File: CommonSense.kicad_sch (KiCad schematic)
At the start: 33 parts, among them J1 Conn_02x04_Counter_Clockwise, J2 Conn_01x02, J3 Conn_01x02, U1 NRF52810-QFAA-R7, U2 SHT41-AD1B-R2, Y1 ECS-.327-12.5-12R-TR, Y2 ABM11W-32.0000MHZ-7-D1X-T3

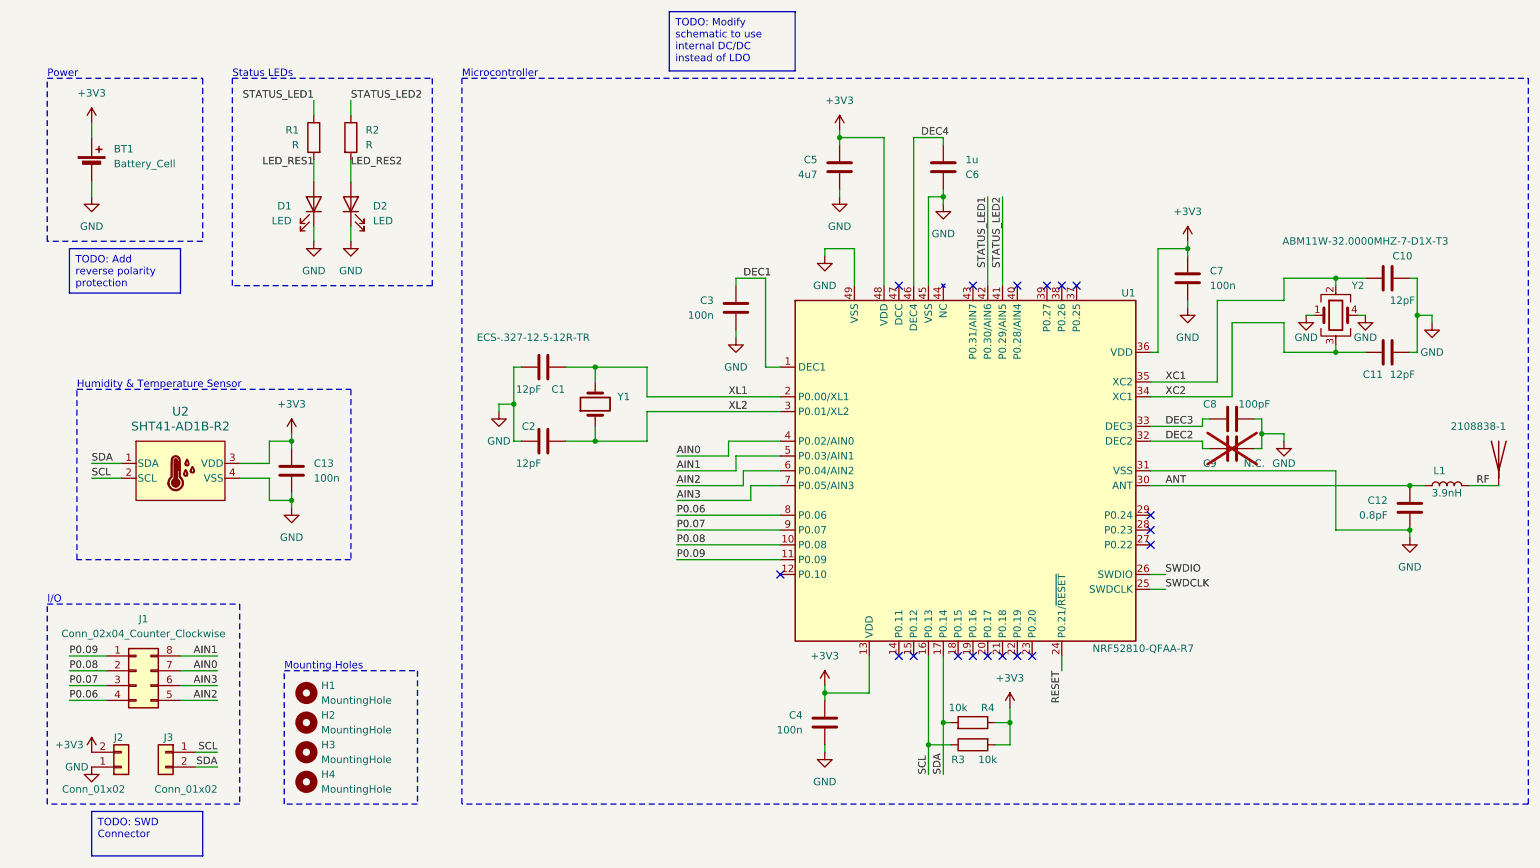
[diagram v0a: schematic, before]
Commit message: Add SWD connector; Add text on silkscreen
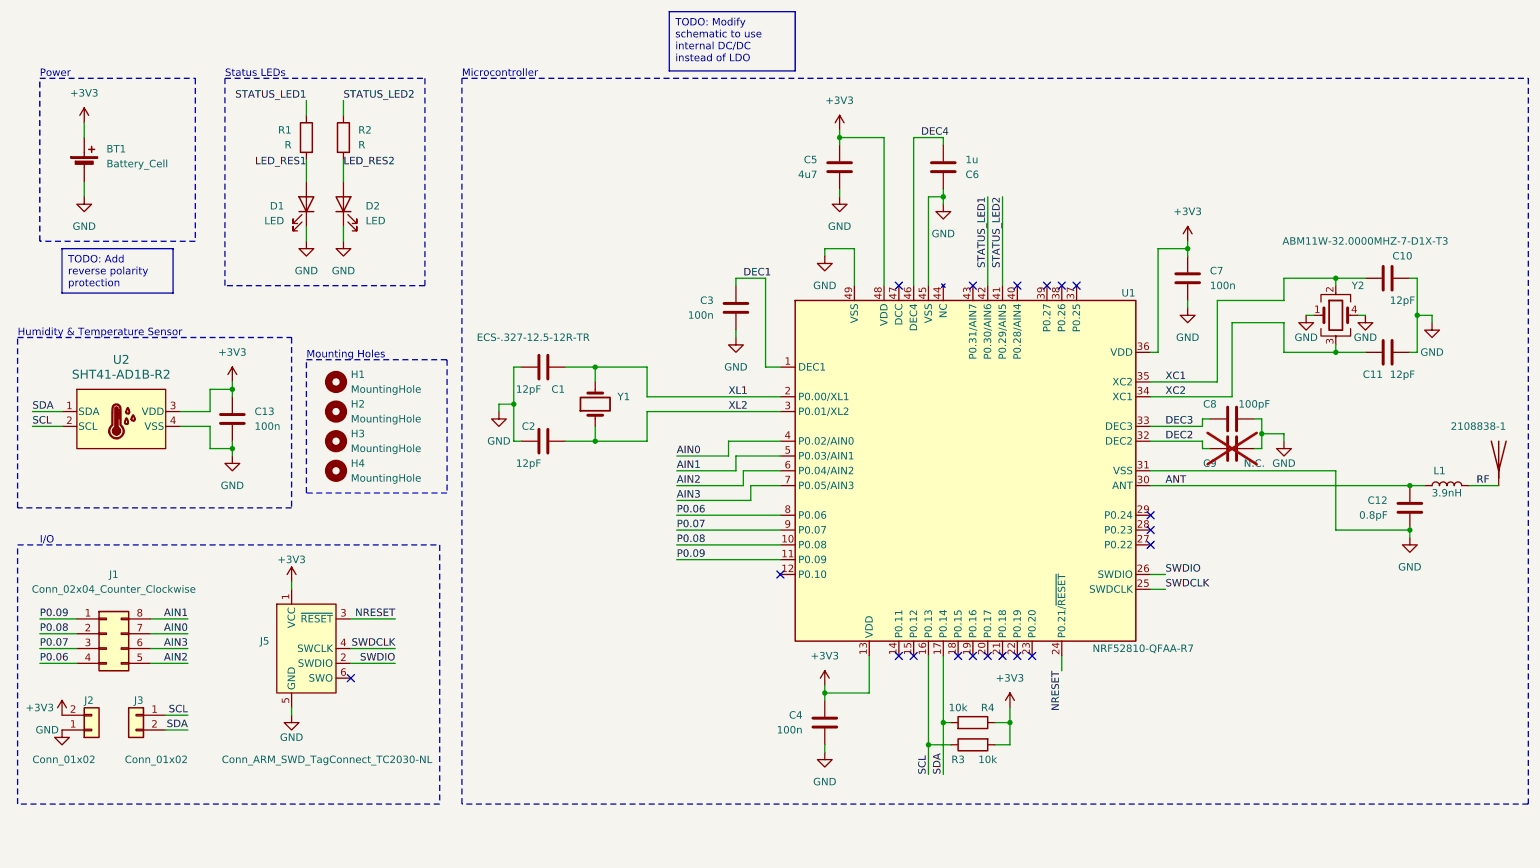
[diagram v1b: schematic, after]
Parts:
- added J5: Conn_ARM_SWD_TagConnect_TC2030-NL, Connector:Tag-Connect_TC2030-IDC-NL_2x03_P1.27mm_Vertical, symbol Connector:Conn_ARM_SWD_TagConnect_TC2030-NL
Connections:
- net +3V3: now also J5.1 (VCC)
- net GND: now also J5.5 (GND)
- net SWDCLK: now also J5.4 (SWCLK)
- net SWDIO: now also J5.2 (SWDIO)
- net RESET renamed NRESET
- net NRESET: now also J5.3 (~{RESET})
- no-connect marks 18 -> 19
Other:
- moved on the sheet: BT1, C13, D1, D2, H1, H2, H3, H4, J1, J2, J3, R1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

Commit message: Remove one status LED and move the other one; Fix text placement of 3V3 GND
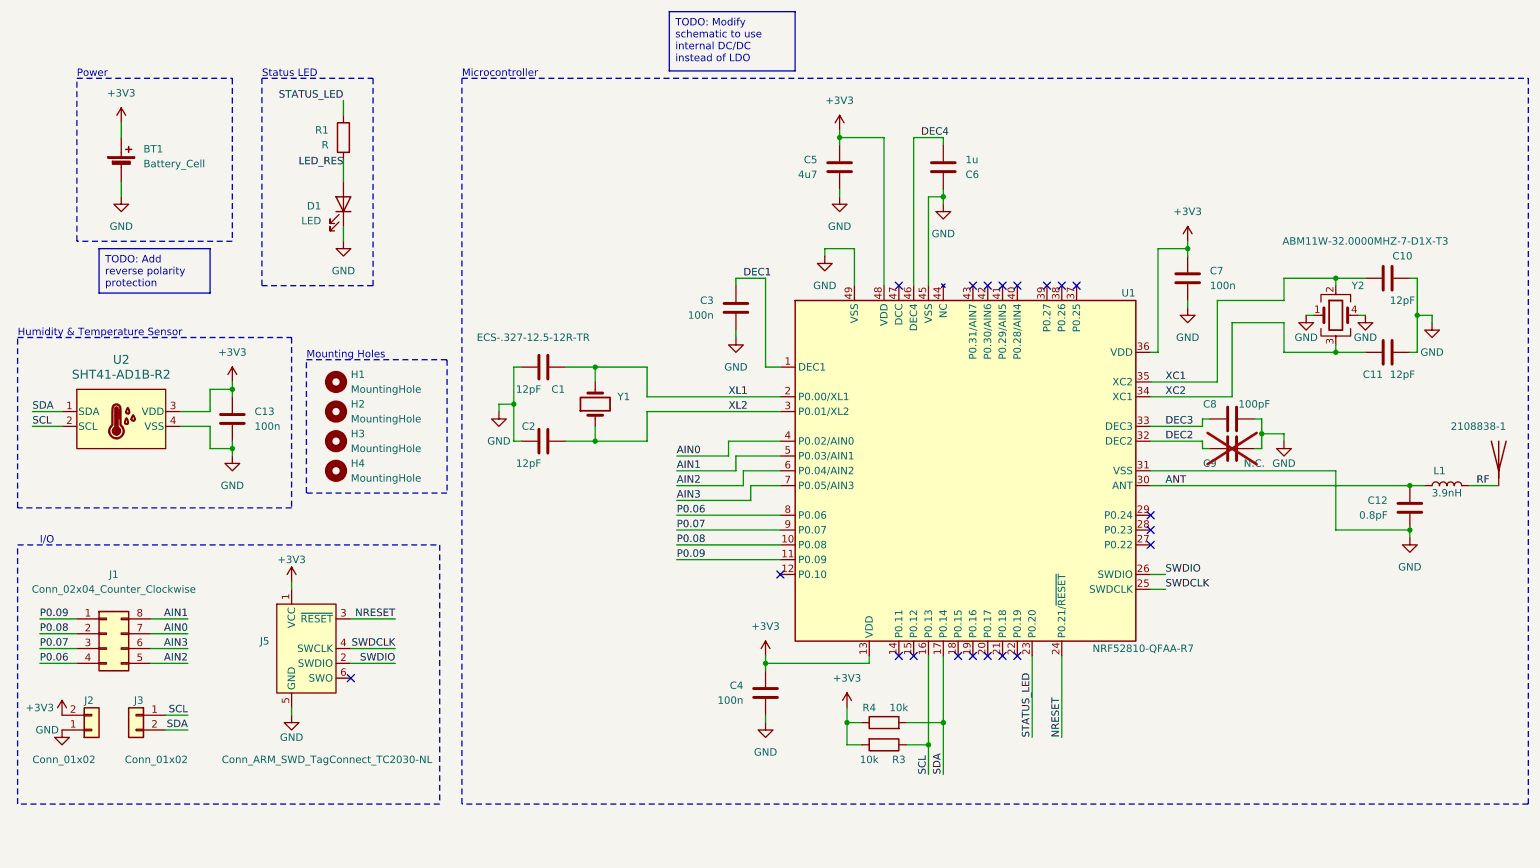
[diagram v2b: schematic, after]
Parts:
- removed D2: LED, Resistor_SMD:R_0603_1608Metric, symbol Device:LED
- removed R2: R, Resistor_SMD:R_0603_1608Metric, symbol Device:R
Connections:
- net STATUS_LED: now reaches U1.23 (P0.20)
- net STATUS_LED: now also R1.1
- net LED_RES1 renamed LED_RES
- net STATUS_LED1: no longer names the net of U1.42 (P0.30/AIN6)
- net STATUS_LED1: no longer R1.1
- net STATUS_LED2: no longer names the net of U1.41 (P0.29/AIN5)
- no-connect marks 19 -> 20
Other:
- note added: "Status LED"
- note removed: "Status LEDs"
- moved on the sheet: BT1, C4, D1, R1, R3, R4

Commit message: Add inductors and clean up bottom part of PCB
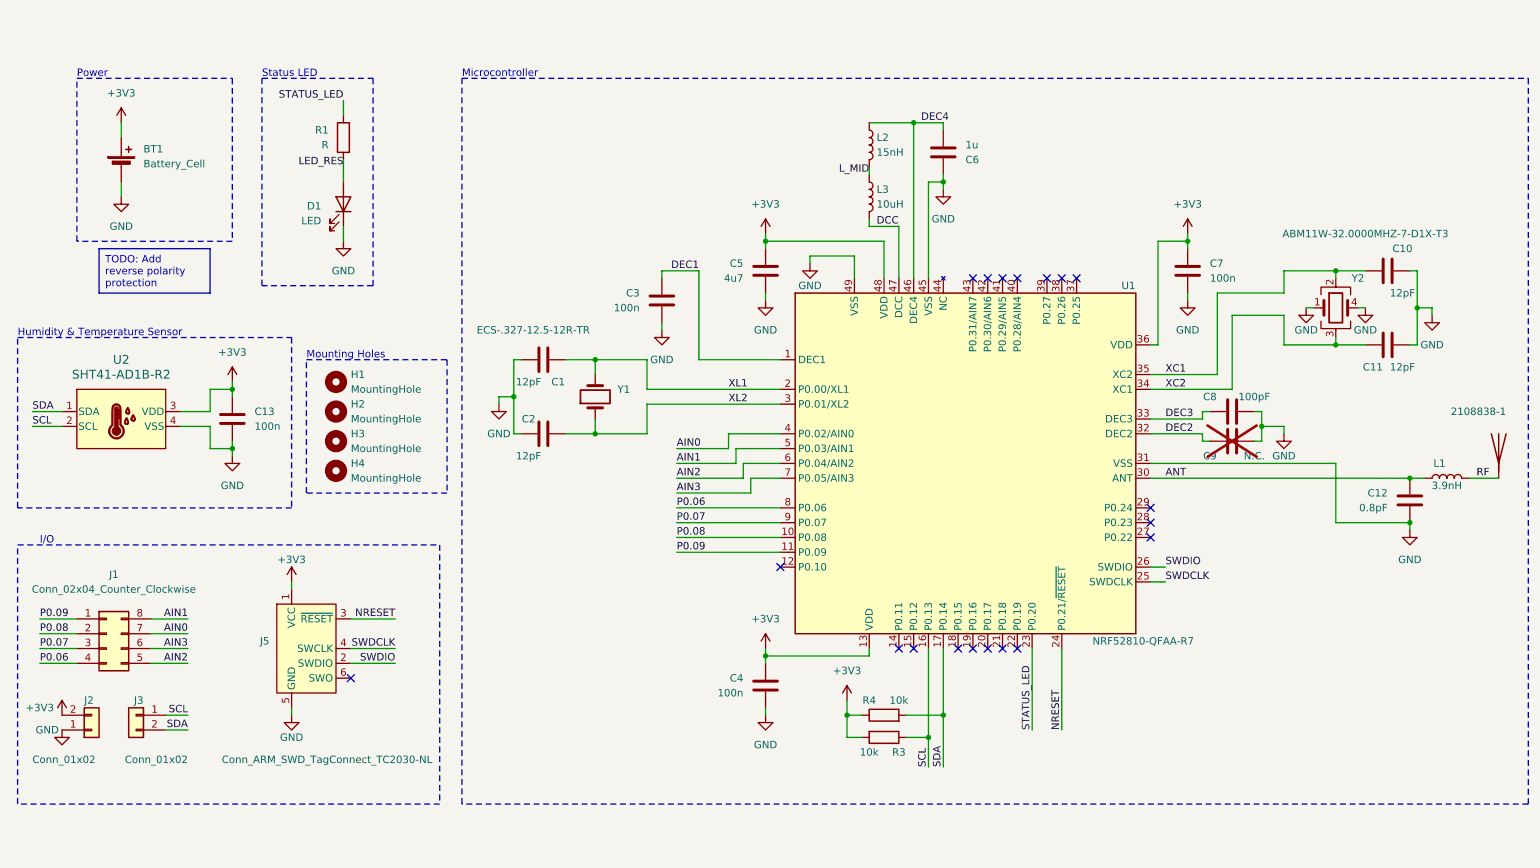
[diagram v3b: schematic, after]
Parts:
- added L2: 15nH, Inductor_SMD:L_0603_1608Metric, symbol Device:L
- added L3: 10uH, Inductor_SMD:L_0603_1608Metric, symbol Device:L
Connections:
- net DEC4: now also L2.1
- net DCC: now reaches U1.47 (DCC)
- net DCC: now also L3.2
- new net L_MID: L2.2, L3.1
- no-connect marks 20 -> 19
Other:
- moved on the sheet: 2108838-1, C1, C10, C11, C12, C2, C3, C4, C5, C6, C7, C8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

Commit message: Add reverse polarity protection diodes; Start cleaning up top part of PCB
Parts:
- added D2, D3: CDBU0130L-HF, Diode_SMD:D_0603_1608Metric, symbol Device:D_Schottky
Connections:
- net +3V3 renamed +3V0
- net +3V0: now also D2.1 (K), D3.1 (K); no longer BT1.1 (+), J2.2 (Pin_2)
- new net +BATT: BT1.1 (+), D2.2 (A), D3.2 (A), J2.2 (Pin_2)
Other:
- moved on the sheet: BT1

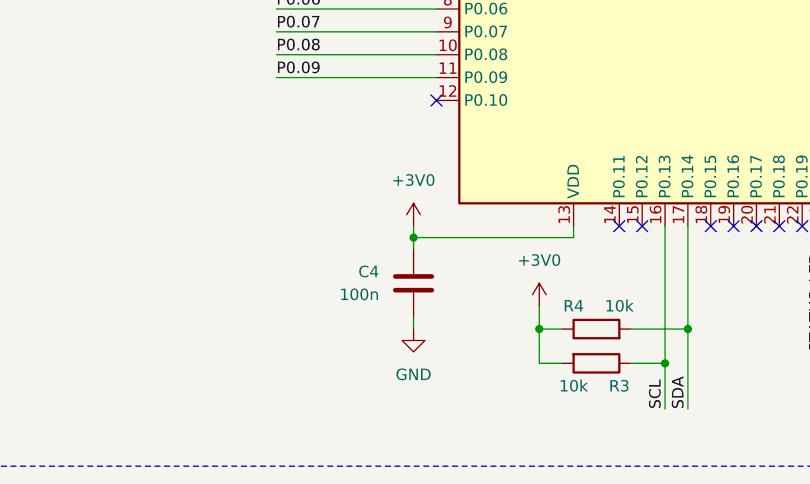
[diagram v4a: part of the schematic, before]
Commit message: Add additional 1u bypass capacitor
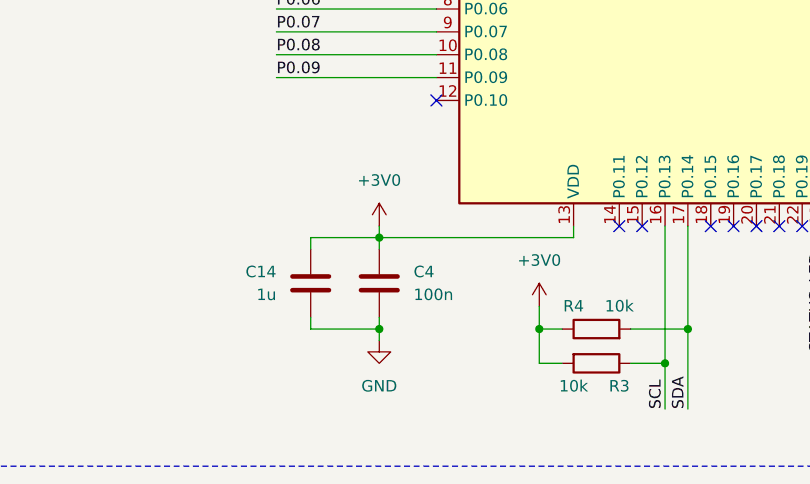
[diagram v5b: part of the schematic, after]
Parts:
- added C14: 1u, Capacitor_SMD:C_0603_1608Metric, symbol Device:C
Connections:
- net +3V0: now also C14.2
- net GND: now also C14.1
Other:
- moved on the sheet: C4
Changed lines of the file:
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@@
 (kicad_sch (version 20230121) (generator eeschema)
   (paper "A4")
+  (junction (at 140.97 142.24) (diameter 0) (color 0 0 0 0)
+  )
   (junction (at 242.57 66.04) (diameter 0) (color 0 0 0 0)
   )
@@
   (junction (at 255.27 109.22) (diameter 0) (color 0 0 0 0)
   )
-  (junction (at 144.78 132.08) (diameter 0) (color 0 0 0 0)
+  (junction (at 140.97 132.08) (diameter 0) (color 0 0 0 0)
   )
   (junction (at 175.26 50.8) (diameter 0) (color 0 0 0 0)
@@
     (stroke (width 0) (type default))
   )
-  (wire (pts (xy 144.78 140.97) (xy 144.78 142.24))
+  (wire (pts (xy 140.97 140.97) (xy 140.97 142.24))
     (stroke (width 0) (type default))
   )
@@
     (stroke (width 0) (type default))
   )
+  (wire (pts (xy 140.97 132.08) (xy 140.97 133.35))
+    (stroke (width 0) (type default))
+  )
   (wire (pts (xy 129.54 109.22) (xy 147.32 109.22))
     (stroke (width 0) (type default))
@@
     (stroke (width 0) (type default))
   )
-  (wire (pts (xy 144.78 132.08) (xy 144.78 133.35))
-    (stroke (width 0) (type default))
-  )
   (wire (pts (xy 233.68 93.98) (xy 233.68 92.71))
     (stroke (width 0) (type default))
@@
     (stroke (width 0) (type default))
   )
+  (wire (pts (xy 133.35 132.08) (xy 140.97 132.08))
+    (stroke (width 0) (type default))
+  )
   (wire (pts (xy 53.34 86.36) (xy 53.34 87.63))
     (stroke (width 0) (type default))
@@
     (stroke (width 0) (type default))
   )
-  (wire (pts (xy 144.78 130.81) (xy 144.78 132.08))
+  (wire (pts (xy 140.97 130.81) (xy 140.97 132.08))
     (stroke (width 0) (type default))
   )
@@
     (stroke (width 0) (type default))
   )
+  (wire (pts (xy 133.35 140.97) (xy 133.35 142.24))
+    (stroke (width 0) (type default))
+  )
   (wire (pts (xy 210.82 101.6) (xy 255.27 101.6))
     (stroke (width 0) (type default))
@@
     (stroke (width 0) (type default))
   )
-  (wire (pts (xy 144.78 132.08) (xy 162.56 132.08))
+  (wire (pts (xy 140.97 132.08) (xy 162.56 132.08))
     (stroke (width 0) (type default))
   )
@@
     (stroke (width 0) (type default))
   )
+  (wire (pts (xy 133.35 133.35) (xy 133.35 132.08))
+    (stroke (width 0) (type default))
+  )
   (wire (pts (xy 124.46 93.98) (xy 124.46 88.9))
     (stroke (width 0) (type default))
@@
     (stroke (width 0) (type default))
   )
+  (wire (pts (xy 140.97 142.24) (xy 140.97 143.51))
+    (stroke (width 0) (type default))
+  )
   (wire (pts (xy 115.57 91.44) (xy 115.57 93.98))
     (stroke (width 0) (type default))
@@
   )
   (wire (pts (xy 99.06 87.63) (xy 101.6 87.63))
+    (stroke (width 0) (type default))
+  )
+  (wire (pts (xy 133.35 142.24) (xy 140.97 142.24))
     (stroke (width 0) (type default))
   )
@@
         (path "/523ef776-806b-43b6-937c-22b5e6ba7731"
           (reference "C10") (unit 1)
+        )
+      )
+    )
+  )
+  (symbol (lib_id "Device:C") (at 133.35 137.16 0) (mirror x) (unit 1)
+    (in_bom yes) (on_board yes) (dnp no) (fields_autoplaced)
+    (property "Reference" "C14" (at 129.54 135.89 0)
+      (effects (font (size 1.27 1.27)) (justify right))
+    )
+    (property "Value" "1u" (at 129.54 138.43 0)
+      (effects (font (size 1.27 1.27)) (justify right))
+    )
+    (property "Footprint" "Capacitor_SMD:C_0603_1608Metric" (at 134.3152 133.35 0)
+      (effects (font (size 1.27 1.27)) hide)
+    )
+    (property "Datasheet" "~" (at 133.35 137.16 0)
+      (effects (font (size 1.27 1.27)) hide)
+    )
+    (pin "1")
+    (pin "2")
+    (instances
+      (project "CommonSense"
+        (path "/38fbf0b5-ae68-401e-b1a9-e916ed01fc13"
+          (reference "C14") (unit 1)
+        )
+      )
+      (project "nodemcu_humidity_shield"
+        (path "/523ef776-806b-43b6-937c-22b5e6ba7731"
+          (reference "C13") (unit 1)
         )
       )
@@
     )
   )
-  (symbol (lib_id "power:GND") (at 144.78 142.24 0) (unit 1)
-    (in_bom yes) (on_board yes) (dnp no) (fields_autoplaced)
-    (property "Reference" "#PWR09" (at 144.78 148.59 0)
-      (effects (font (size 1.27 1.27)) hide)
-    )
-    (property "Value" "GND" (at 144.78 147.32 0)
-      (effects (font (size 1.27 1.27)))
-    )
-    (property "Footprint" "" (at 144.78 142.24 0)
-      (effects (font (size 1.27 1.27)) hide)
-    )
-    (property "Datasheet" "" (at 144.78 142.24 0)
+  (symbol (lib_id "power:GND") (at 140.97 143.51 0) (unit 1)
+    (in_bom yes) (on_board yes) (dnp no) (fields_autoplaced)
+    (property "Reference" "#PWR09" (at 140.97 149.86 0)
+      (effects (font (size 1.27 1.27)) hide)
+    )
+    (property "Value" "GND" (at 140.97 148.59 0)
+      (effects (font (size 1.27 1.27)))
+    )
+    (property "Footprint" "" (at 140.97 143.51 0)
+      (effects (font (size 1.27 1.27)) hide)
+    )
+    (property "Datasheet" "" (at 140.97 143.51 0)
       (effects (font (size 1.27 1.27)) hide)
     )
@@
     )
   )
-  (symbol (lib_id "power:+3V0") (at 144.78 130.81 0) (unit 1)
-    (in_bom yes) (on_board yes) (dnp no) (fields_autoplaced)
-    (property "Reference" "#PWR024" (at 144.78 134.62 0)
-      (effects (font (size 1.27 1.27)) hide)
-    )
-    (property "Value" "+3V0" (at 144.78 125.73 0)
-      (effects (font (size 1.27 1.27)))
-    )
-    (property "Footprint" "" (at 144.78 130.81 0)
-      (effects (font (size 1.27 1.27)) hide)
-    )
-    (property "Datasheet" "" (at 144.78 130.81 0)
+  (symbol (lib_id "power:+3V0") (at 140.97 130.81 0) (unit 1)
+    (in_bom yes) (on_board yes) (dnp no) (fields_autoplaced)
+    (property "Reference" "#PWR024" (at 140.97 134.62 0)
+      (effects (font (size 1.27 1.27)) hide)
+    )
+    (property "Value" "+3V0" (at 140.97 125.73 0)
+      (effects (font (size 1.27 1.27)))
+    )
+    (property "Footprint" "" (at 140.97 130.81 0)
+      (effects (font (size 1.27 1.27)) hide)
+    )
+    (property "Datasheet" "" (at 140.97 130.81 0)
       (effects (font (size 1.27 1.27)) hide)
     )
@@
     )
   )
-  (symbol (lib_id "Device:C") (at 144.78 137.16 0) (mirror x) (unit 1)
-    (in_bom yes) (on_board yes) (dnp no) (fields_autoplaced)
-    (property "Reference" "C4" (at 140.97 135.89 0)
+  (symbol (lib_id "Device:C") (at 140.97 137.16 180) (unit 1)
+    (in_bom yes) (on_board yes) (dnp no)
+    (property "Reference" "C4" (at 144.78 135.89 0)
       (effects (font (size 1.27 1.27)) (justify right))
     )
-    (property "Value" "100n" (at 140.97 138.43 0)
+    (property "Value" "100n" (at 144.78 138.43 0)
       (effects (font (size 1.27 1.27)) (justify right))
     )
-    (property "Footprint" "Capacitor_SMD:C_0603_1608Metric" (at 145.7452 133.35 0)
-      (effects (font (size 1.27 1.27)) hide)
-    )
-    (property "Datasheet" "~" (at 144.78 137.16 0)
-      (effects (font (size 1.27 1.27)) hide)
-    )
+    (property "Footprint" "Capacitor_SMD:C_0603_1608Metric" (at 140.0048 133.35 0)
+      (effects (font (size 1.27 1.27)) hide)
+    )
+    (property "Datasheet" "~" (at 140.97 137.16 0)
+      (effects (font (size 1.27 1.27)) hide)
+    )
